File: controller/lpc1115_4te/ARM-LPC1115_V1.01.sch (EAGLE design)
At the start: 100 parts, among them IC1 LPC1115, IC2 BD9G101, Q2 BCP52, Q3 BC856, Q4 12MHz, T1 BC547C

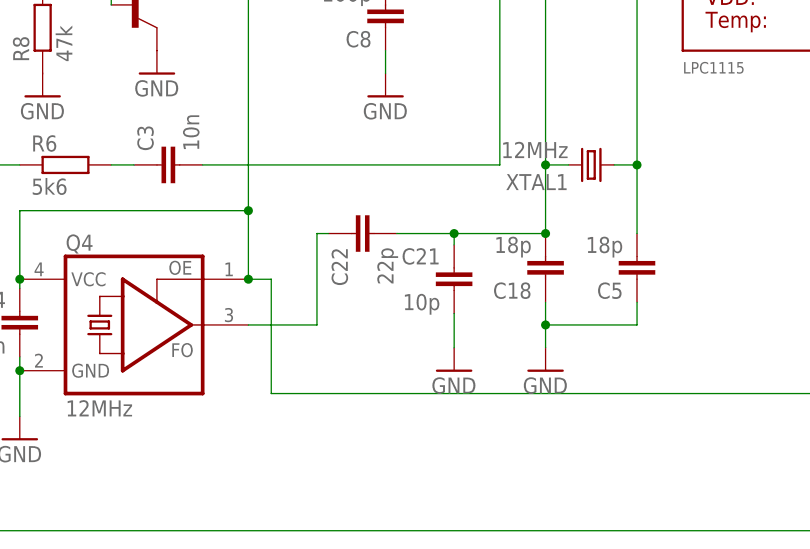
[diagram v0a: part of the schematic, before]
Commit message: cap dividor value changed
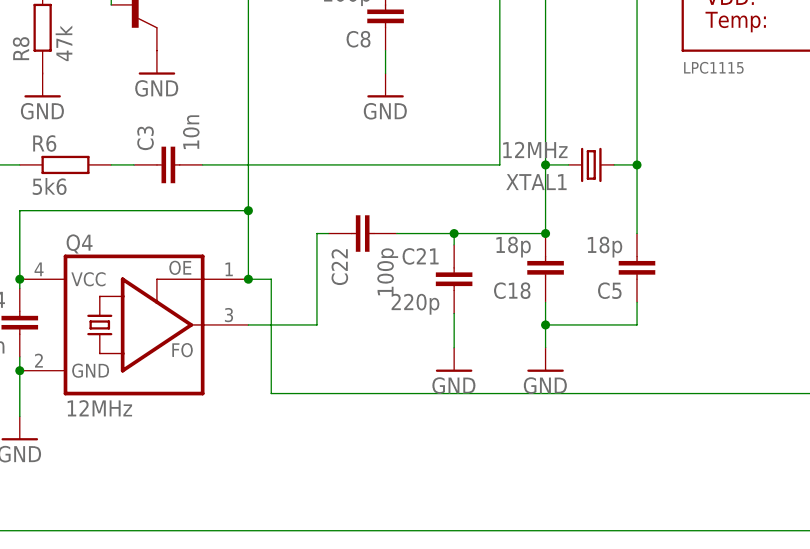
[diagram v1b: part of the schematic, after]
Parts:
- C21: value 10p -> 220p
- C22: value 22p -> 100p
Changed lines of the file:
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@@
 <part name="D8" library="semicon-smd-ipc" deviceset="D-" device="SMB"/>
 <part name="C20" library="rcl" deviceset="C-EU" device="C1206"/>
-<part name="C21" library="rcl" deviceset="C-EU" device="C1206" value="10p"/>
-<part name="C22" library="rcl" deviceset="C-EU" device="C1206" value="22p"/>
+<part name="C21" library="rcl" deviceset="C-EU" device="C1206" value="220p"/>
+<part name="C22" library="rcl" deviceset="C-EU" device="C1206" value="100p"/>
 <part name="GND11" library="supply1" deviceset="GND" device=""/>
 </parts>
